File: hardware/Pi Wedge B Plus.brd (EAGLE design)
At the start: 73.7 x 63.5 mm, 15 parts

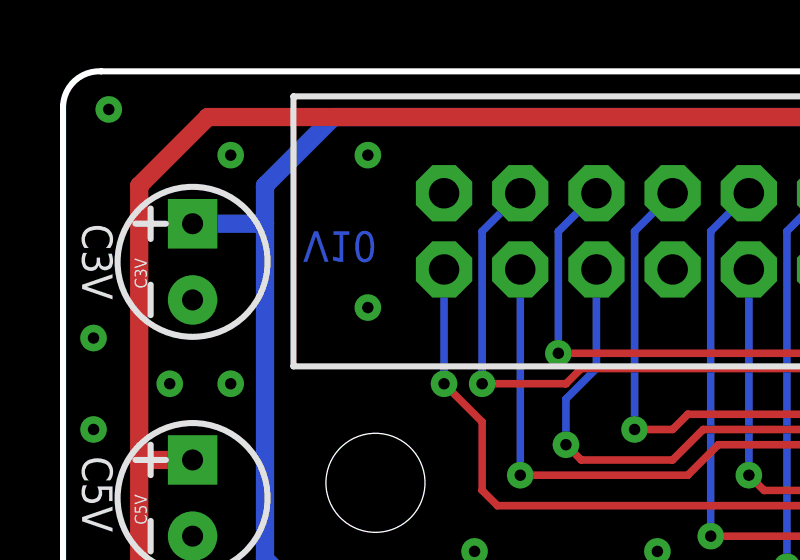
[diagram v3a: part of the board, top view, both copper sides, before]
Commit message: Fixing kit soldermask on 17-pin headers.
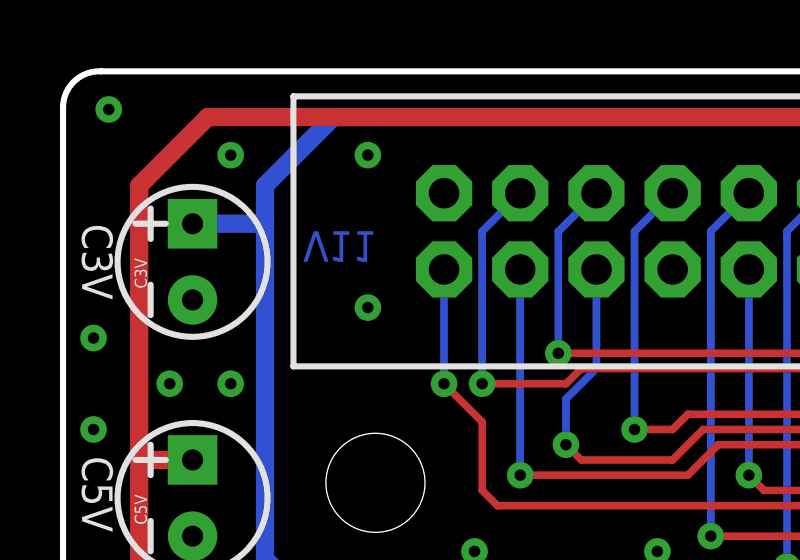
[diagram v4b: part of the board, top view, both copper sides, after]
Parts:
- flipped U$4 to the bottom
- flipped U$5 to the bottom
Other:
- board text added: "V11"
- board text removed: "V10"
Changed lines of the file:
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@@
 <layer number="23" name="tOrigins" color="15" fill="1" visible="yes" active="yes"/>
 <layer number="24" name="bOrigins" color="15" fill="1" visible="yes" active="yes"/>
-<layer number="25" name="tNames" color="7" fill="1" visible="no" active="yes"/>
-<layer number="26" name="bNames" color="7" fill="1" visible="no" active="yes"/>
-<layer number="27" name="tValues" color="7" fill="1" visible="no" active="yes"/>
-<layer number="28" name="bValues" color="7" fill="1" visible="no" active="yes"/>
-<layer number="29" name="tStop" color="7" fill="3" visible="no" active="yes"/>
-<layer number="30" name="bStop" color="7" fill="6" visible="no" active="yes"/>
+<layer number="25" name="tNames" color="7" fill="1" visible="yes" active="yes"/>
+<layer number="26" name="bNames" color="7" fill="1" visible="yes" active="yes"/>
+<layer number="27" name="tValues" color="7" fill="1" visible="yes" active="yes"/>
+<layer number="28" name="bValues" color="7" fill="1" visible="yes" active="yes"/>
+<layer number="29" name="tStop" color="7" fill="3" visible="yes" active="yes"/>
+<layer number="30" name="bStop" color="7" fill="6" visible="yes" active="yes"/>
 <layer number="31" name="tCream" color="7" fill="4" visible="no" active="yes"/>
 <layer number="32" name="bCream" color="7" fill="5" visible="no" active="yes"/>
@@
 <layer number="43" name="vRestrict" color="2" fill="10" visible="no" active="yes"/>
 <layer number="44" name="Drills" color="7" fill="1" visible="no" active="yes"/>
-<layer number="45" name="Holes" color="7" fill="1" visible="yes" active="yes"/>
+<layer number="45" name="Holes" color="7" fill="1" visible="no" active="yes"/>
 <layer number="46" name="Milling" color="3" fill="1" visible="no" active="yes"/>
 <layer number="47" name="Measures" color="7" fill="1" visible="no" active="yes"/>
@@
 <wire x1="0" y1="62.357" x2="0" y2="46.101" width="0.2032" layer="20"/>
 <wire x1="0" y1="46.101" x2="1.27" y2="44.704" width="0.2032" layer="20" curve="90"/>
-<text x="8.001" y="58.166" size="1.016" layer="16" font="vector" ratio="20" rot="SMR180">V10</text>
+<text x="8.001" y="58.166" size="1.016" layer="16" font="vector" ratio="20" rot="SMR180">V11</text>
 <text x="31.75" y="1.524" size="1.016" layer="21" font="vector" ratio="19" rot="SR0" align="center-right">GND</text>
 <text x="36.576" y="25.654" size="2.032" layer="21" font="vector" ratio="19" rot="SR90" align="bottom-center">Pi Wedge B+</text>
@@
 <dimension x1="0" y1="69.977" x2="63.246" y2="69.977" x3="31.623" y3="78.74" textsize="1.778" textratio="15" layer="51" unit="inch"/>
 <dimension x1="73.66" y1="0" x2="73.66" y2="63.5" x3="82.677" y3="31.75" textsize="1.778" textratio="15" layer="51" unit="inch"/>
+<text x="31.75" y="1.524" size="1.016" layer="22" font="vector" ratio="19" rot="SMR0" align="center-left">GND</text>
+<text x="31.75" y="21.844" size="1.016" layer="22" font="vector" ratio="19" rot="SMR0" align="center-left">CE0</text>
+<text x="31.75" y="24.384" size="1.016" layer="22" font="vector" ratio="19" rot="SMR0" align="center-left">CE1</text>
+<text x="31.75" y="19.304" size="1.016" layer="22" font="vector" ratio="19" rot="SMR0" align="center-left">MOSI</text>
+<text x="31.75" y="16.764" size="1.016" layer="22" font="vector" ratio="19" rot="SMR0" align="center-left">MISO</text>
+<text x="31.75" y="14.224" size="1.016" layer="22" font="vector" ratio="19" rot="SMR0" align="center-left">SCK</text>
+<text x="31.75" y="11.684" size="1.016" layer="22" font="vector" ratio="19" rot="SMR0" align="center-left">RXI</text>
+<text x="31.75" y="9.144" size="1.016" layer="22" font="vector" ratio="19" rot="SMR0" align="center-left">TXO</text>
+<text x="31.75" y="6.604" size="1.016" layer="22" font="vector" ratio="19" rot="SMR0" align="center-left">5V</text>
+<text x="31.75" y="4.064" size="1.016" layer="22" font="vector" ratio="19" rot="SMR0" align="center-left">3.3V</text>
+<text x="31.75" y="26.924" size="1.016" layer="22" font="vector" ratio="19" rot="SMR0" align="center-left">G4</text>
+<text x="31.75" y="29.464" size="1.016" layer="22" font="vector" ratio="19" rot="SMR0" align="center-left">G5</text>
+<text x="31.75" y="32.004" size="1.016" layer="22" font="vector" ratio="19" rot="SMR0" align="center-left">G6</text>
+<text x="31.75" y="34.544" size="1.016" layer="22" font="vector" ratio="19" rot="SMR0" align="center-left">G12</text>
+<text x="31.75" y="37.084" size="1.016" layer="22" font="vector" ratio="19" rot="SMR0" align="center-left">G13</text>
+<text x="31.75" y="39.624" size="1.016" layer="22" font="vector" ratio="19" rot="SMR0" align="center-left">G16</text>
+<text x="31.75" y="42.164" size="1.016" layer="22" font="vector" ratio="19" rot="SMR0" align="center-left">G17</text>
+<text x="41.91" y="16.764" size="1.016" layer="22" font="vector" ratio="19" rot="SMR0" align="center-right">SCL</text>
+<text x="41.91" y="14.224" size="1.016" layer="22" font="vector" ratio="19" rot="SMR0" align="center-right">SDA</text>
+<text x="41.91" y="4.064" size="1.016" layer="22" font="vector" ratio="19" rot="SMR0" align="center-right">3.3V</text>
+<text x="41.91" y="9.144" size="1.016" layer="22" font="vector" ratio="19" rot="SMR0" align="center-right">IDSD</text>
+<text x="41.91" y="42.164" size="1.016" layer="22" font="vector" ratio="19" rot="SMR0" align="center-right">G18</text>
+<text x="41.91" y="32.004" size="1.016" layer="22" font="vector" ratio="19" rot="SMR0" align="center-right">G22</text>
+<text x="41.91" y="29.464" size="1.016" layer="22" font="vector" ratio="19" rot="SMR0" align="center-right">G23</text>
+<text x="41.91" y="26.924" size="1.016" layer="22" font="vector" ratio="19" rot="SMR0" align="center-right">G24</text>
+<text x="41.91" y="24.384" size="1.016" layer="22" font="vector" ratio="19" rot="SMR0" align="center-right">G25</text>
+<text x="41.91" y="19.304" size="1.016" layer="22" font="vector" ratio="19" rot="SMR0" align="center-right">G27</text>
+<text x="41.91" y="1.524" size="1.016" layer="22" font="vector" ratio="19" rot="SMR0" align="center-right">GND</text>
+<text x="41.91" y="6.604" size="1.016" layer="22" font="vector" ratio="19" rot="SMR0" align="center-right">5V</text>
+<text x="41.91" y="11.684" size="1.016" layer="22" font="vector" ratio="19" rot="SMR0" align="center-right">IDSC</text>
+<text x="41.91" y="21.844" size="1.016" layer="22" font="vector" ratio="19" rot="SMR0" align="center-right">G26</text>
+<text x="41.91" y="39.624" size="1.016" layer="22" font="vector" ratio="19" rot="SMR0" align="center-right">G19</text>
+<text x="41.91" y="37.084" size="1.016" layer="22" font="vector" ratio="19" rot="SMR0" align="center-right">G20</text>
+<text x="41.91" y="34.544" size="1.016" layer="22" font="vector" ratio="19" rot="SMR0" align="center-right">G21</text>
 </plain>
 <attributes>
@@
 <element name="U$2" library="SparkFun-Aesthetics" package="BREADBOARD_SPACING" value="BREADBOARD_PATTERN" x="36.83" y="66.294"/>
 <element name="U$3" library="SparkFun-Boards" package="2X20-SHROUDED" value="RASPBERRYPI-B+-GPIO" x="36.83" y="58.166" rot="R270"/>
-<element name="U$4" library="SparkFun-Connectors" package="1X17_NO_SILK_KIT" value="M17KIT" x="33.02" y="1.524" rot="R90"/>
-<element name="U$5" library="SparkFun-Connectors" package="1X17_NO_SILK_KIT" value="M17KIT" x="40.64" y="1.524" rot="R90"/>
+<element name="U$4" library="SparkFun-Connectors" package="1X17_NO_SILK_KIT" value="M17KIT" x="33.02" y="1.524" rot="MR90"/>
+<element name="U$5" library="SparkFun-Connectors" package="1X17_NO_SILK_KIT" value="M17KIT" x="40.64" y="1.524" rot="MR90"/>
 <element name="LOGO2" library="SparkFun-Aesthetics" package="SFE_LOGO_NAME_FLAME_.2" value="SFE_LOGO_NAME_FLAME.2_INCH" x="48.006" y="44.704" rot="MR0"/>
 </elements>

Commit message: Review updates
Based on Pete Lewis's comments.
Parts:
- removed JP5: LOGO-SFESK, SparkFun:SFE-LOGO-FLAME
- removed U$1: OSHW-LOGOS, SparkFun:OSHW-LOGO-S
- removed U$5: M17KIT, SparkFun-Connectors:1X17_NO_SILK_KIT
- added LOGO3, LOGO4: SFE_LOGO_FLAME.1_INCH, SparkFun-Aesthetics:SFE_LOGO_FLAME_.1
- added LOGO5: OSHW-LOGOS, SparkFun-Aesthetics:OSHW-LOGO-S
- JP1: value LOGO-SFESK -> FTDI_DEVICE; device SparkFun:SFE-LOGO-FLAME -> SparkFun-Connectors:FTDI_DEVICE_SIDE
- JP4: value FTDI_DEVICE -> M17KIT; device SparkFun-Connectors:FTDI_DEVICE_SIDE -> SparkFun-Connectors:1X17_NO_SILK_KIT
- moved JP1 63.2 mm to (72.4, 54.1)
- moved JP4 61.4 mm to (40.6, 1.52), flipped to the bottom
- renumbered U$3 to JP2, U$4 to JP3
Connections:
- net 3.3V: now also JP4.2; no longer U$5.2
- net 5V: now also JP4.3; no longer U$5.3
- net GND: now also JP1.P$6, JP4.1; no longer JP4.P$6, U$5.1
- net GP18: now also JP4.17; no longer U$5.17
- net GP19: now also JP4.16; no longer U$5.16
- net GP20: now also JP4.15; no longer U$5.15
- net GP21: now also JP4.14; no longer U$5.14
- net GP22: now also JP4.13; no longer U$5.13
- net GP23: now also JP4.12; no longer U$5.12
- net GP24: now also JP4.11; no longer U$5.11
- net GP25: now also JP4.10; no longer U$5.10
- net GP26: now also JP4.9; no longer U$5.9
- net GP27: now also JP4.8; no longer U$5.8
- net ID_SC: now also JP4.5; no longer U$5.5
- net ID_SD: now also JP4.4; no longer U$5.4
- net RXI: now also JP1.P$3; no longer JP4.P$3
- net SCL: now also JP4.7; no longer U$5.7
- net SDA: now also JP4.6; no longer U$5.6
- net TXO: now also JP1.P$2; no longer JP4.P$2
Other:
- board text added: "Use with 3.3V FTDI adapter"
